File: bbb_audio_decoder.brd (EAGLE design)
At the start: 110.5 x 100 mm, 183 parts, among them IC1 OPA2134, IC2 LM317, IC3 LM337, IC4 OPA2134, IC5 OPA2134, IC6 OPA2134, P1 PLR135/T9, P9 P9, Q1 BS170, Q2 BS170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

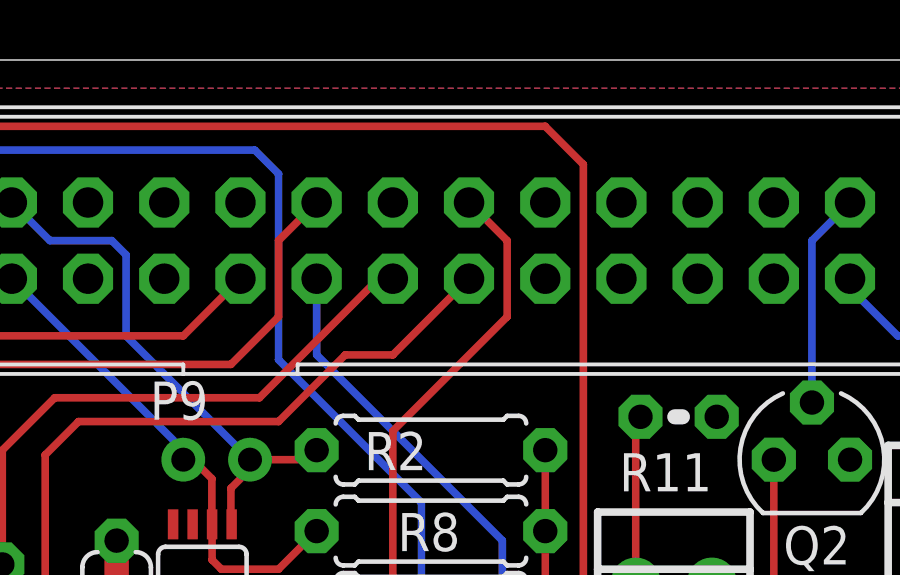
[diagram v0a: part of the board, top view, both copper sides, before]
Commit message: Fix DIR9001 DOUT wrong connection
It was wired to pin 32 in BBB P9, which is VADC. The correct pin is 30.
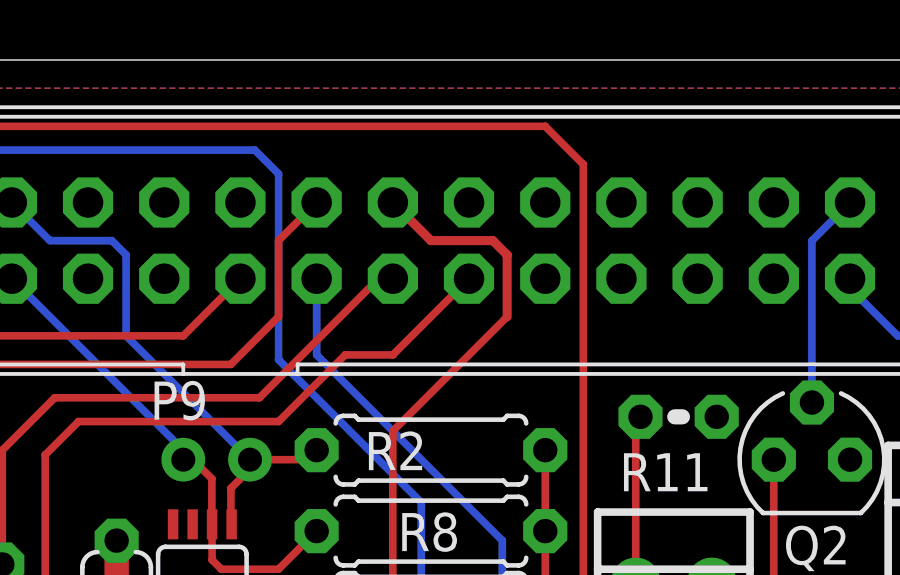
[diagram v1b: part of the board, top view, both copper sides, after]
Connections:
- net DIN: now also P9.30; no longer P9.32
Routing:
- net DIN: track 18.4 -> 20.6 mm
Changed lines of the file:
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@@
 <signal name="DIN">
 <contactref element="R32" pad="1"/>
-<contactref element="P9" pad="32"/>
-<wire x1="85.09" y1="95.25" x2="86.36" y2="93.98" width="0.254" layer="1"/>
-<wire x1="86.36" y1="93.98" x2="86.36" y2="91.44" width="0.254" layer="1"/>
+<contactref element="P9" pad="30"/>
 <wire x1="86.36" y1="91.44" x2="82.55" y2="87.63" width="0.254" layer="1"/>
 <wire x1="82.55" y1="87.63" x2="82.55" y2="81.43875" width="0.254" layer="1"/>
 <wire x1="82.55" y1="81.43875" x2="80.80375" y2="79.6925" width="0.254" layer="1"/>
+<wire x1="86.36" y1="91.44" x2="86.36" y2="93.50375" width="0.3048" layer="1"/>
+<wire x1="86.36" y1="93.50375" x2="85.88375" y2="93.98" width="0.3048" layer="1"/>
+<wire x1="85.88375" y1="93.98" x2="83.82" y2="93.98" width="0.3048" layer="1"/>
+<wire x1="83.82" y1="93.98" x2="82.55" y2="95.25" width="0.3048" layer="1"/>
 </signal>
 <signal name="N$5">

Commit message: Fixes wrong net name
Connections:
- net AHCLKX renamed FSX
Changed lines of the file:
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@@
 <wire x1="78.74" y1="93.98" x2="80.01" y2="95.25" width="0.254" layer="1"/>
 </signal>
-<signal name="AHCLKX">
+<signal name="FSX">
 <contactref element="P9" pad="29"/>
 <contactref element="R35" pad="1"/>

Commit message: Use P9 connector with wiring for slave m-clock
As described from the eaglecustom repo:

> For my purpose, I need to use an external master clock. This is input on
> ahclkr, which is pin 28. For that, the previous pin 28 function, axr2,
> has been moved to axr1, pin 41. And for that, the 'ready' LED that was
> on pin 41 has been removed.
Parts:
- removed Q1: BS170, transistor-small-signal:SOT54E
- removed R10: 120, rcl:0204V
- removed READY: 22-23-2021, con-molex:22-23-2021
- U$1: value P9 -> BEAGLEBONEP9
- renumbered P9 to U$1
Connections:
- removed net N$28: R10.1, READY.1
- removed net N$4: Q1.D, READY.2
- removed net N$93: Q1.G, U$1.41
- net DGND: no longer Q1.S
- net DOUT: now also U$1.41; no longer U$1.28
- net VDD: no longer R10.2
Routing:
- net DOUT: track 25.0 -> 40.2 mm, vias 0 -> 1
- net N$93: track 10.9 -> 0.00 mm
- net N$4: track 5.03 -> 0.00 mm
- net N$28: track 4.32 -> 0.00 mm
- net FSX: track 19.2 -> 20.7 mm
- net N$94: track 7.19 -> 8.25 mm
- net ACLKX: track 27.1 -> 27.8 mm

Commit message: Set DIR9001 SCKO to 512 * Fs
Both PSCKO pins connect to VDD. I need this to drive 8 channel TDM mode
in the mcasp in the Beagle Bone.
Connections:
- net VDD: now also U2.13, U2.14
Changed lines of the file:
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@@
 <contactref element="U$1" pad="4"/>
 <contactref element="U$1" pad="3"/>
+<contactref element="U2" pad="14"/>
+<contactref element="U2" pad="13"/>
 </signal>
 <signal name="DGND">

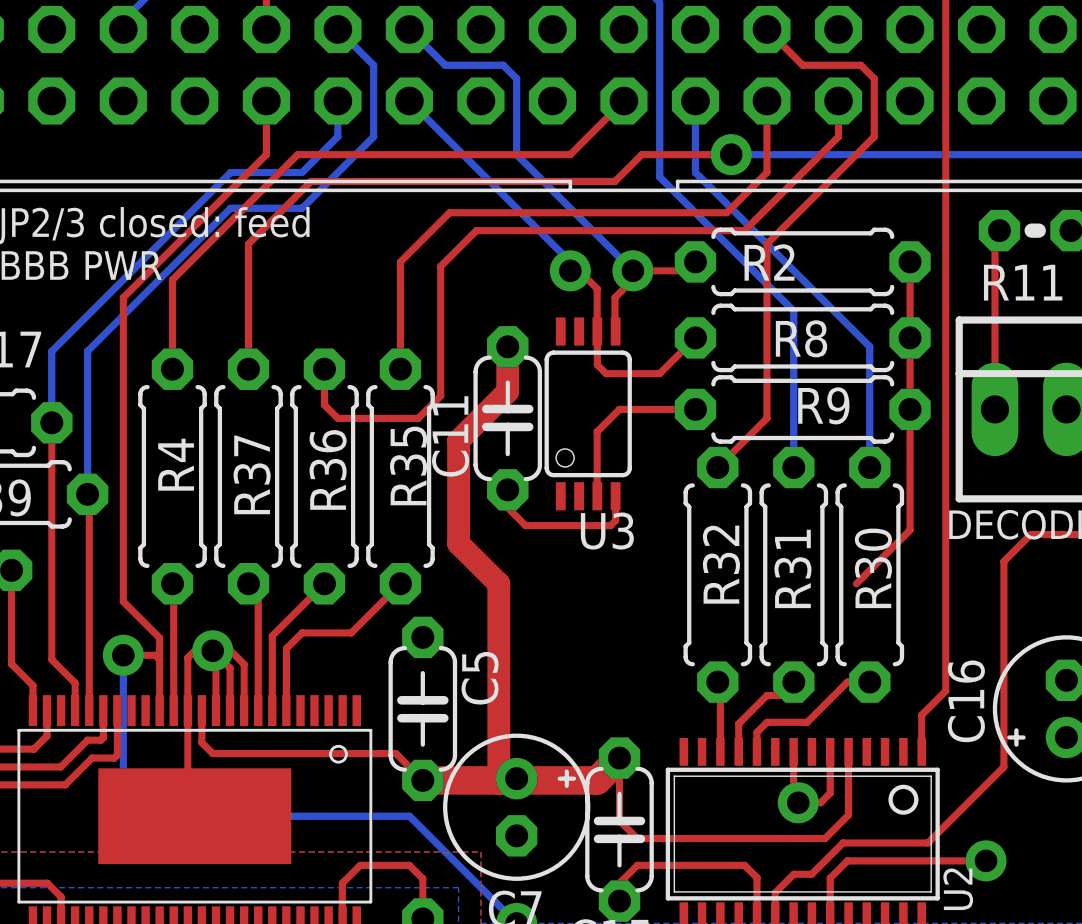
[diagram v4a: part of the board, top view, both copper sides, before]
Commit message: DIR9001 SCKO goes to input of PCM1690 and BBB
This follows commit c6b4b11003516838945a68f4a9d2063d0b8848d0; we now
actually connect the master clock.
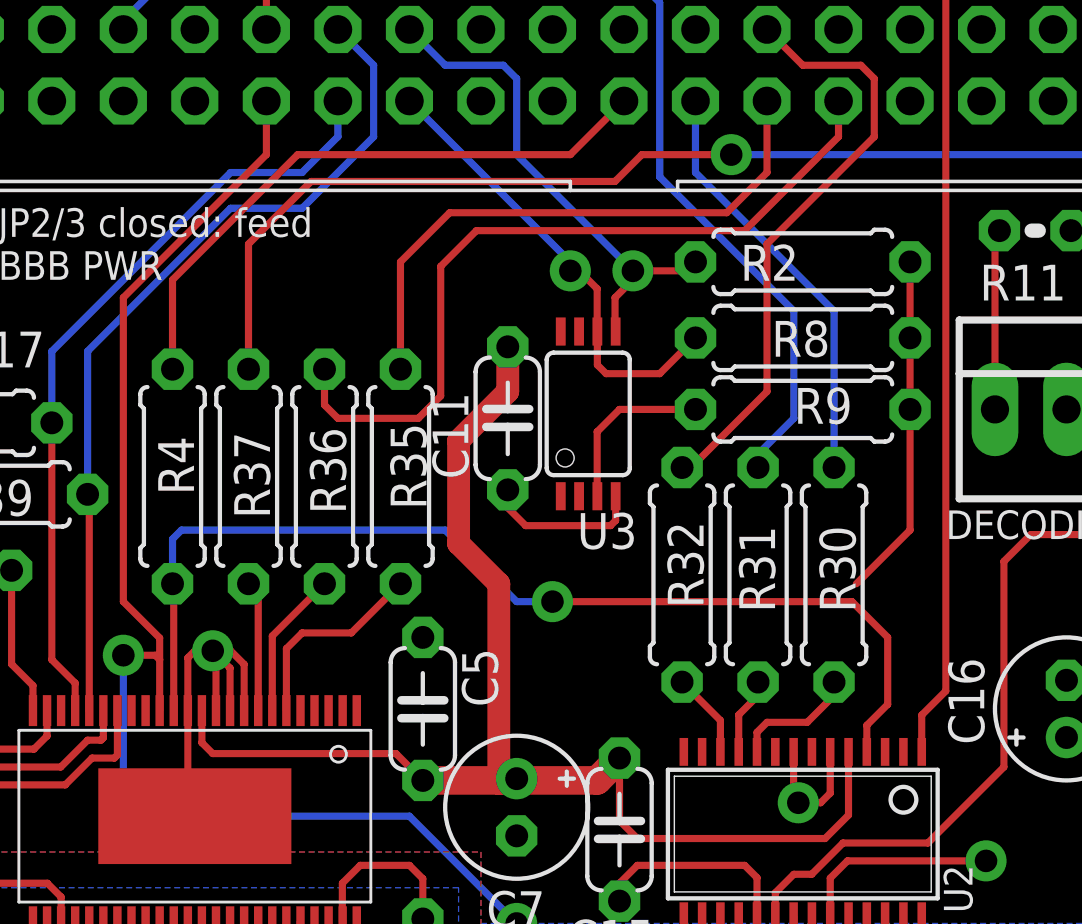
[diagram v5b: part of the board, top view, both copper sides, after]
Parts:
- moved R30 1.27 mm to (84.9, 75.9)
- moved R31 1.27 mm to (82.2, 75.9)
- moved R32 1.27 mm to (79.5, 75.9)
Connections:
- net N$5: now also U2.4
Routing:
- net N$5: track 4.52 -> 37.6 mm, vias 0 -> 1
- net N$52: track 3.57 -> 2.76 mm
- net DIN: track 20.6 -> 21.4 mm
- net ACLKR: track 38.8 -> 39.3 mm
- net N$51: track 2.52 -> 3.04 mm
- net FSR: track 15.6 -> 15.1 mm
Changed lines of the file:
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@@
 <attribute name="VALUE" x="84.455" y="60.96" size="1.27" layer="27" ratio="10" rot="R270"/>
 </element>
-<element name="R30" library="rcl" package="0207/7" value="22" x="86.20125" y="75.8825" smashed="yes" rot="R270">
-<attribute name="NAME" x="85.69325" y="77.62875" size="1.27" layer="25" ratio="10" rot="R270"/>
-<attribute name="VALUE" x="85.64245" y="78.1685" size="1.27" layer="27" ratio="10" rot="R270"/>
-</element>
-<element name="R31" library="rcl" package="0207/7" value="22" x="83.5025" y="75.8825" smashed="yes" rot="R270">
-<attribute name="NAME" x="82.83575" y="77.62875" size="1.27" layer="25" ratio="10" rot="R270"/>
-<attribute name="VALUE" x="82.9437" y="78.1685" size="1.27" layer="27" ratio="10" rot="R270"/>
-</element>
-<element name="R32" library="rcl" package="0207/7" value="22" x="80.80375" y="75.8825" smashed="yes" rot="R270">
-<attribute name="NAME" x="80.29575" y="77.7875" size="1.27" layer="25" ratio="10" rot="R270"/>
-<attribute name="VALUE" x="80.24495" y="78.1685" size="1.27" layer="27" ratio="10" rot="R270"/>
+<element name="R30" library="rcl" package="0207/7" value="22" x="84.93125" y="75.8825" smashed="yes" rot="R270">
+<attribute name="NAME" x="84.42325" y="77.62875" size="1.27" layer="25" ratio="10" rot="R270"/>
+<attribute name="VALUE" x="84.37245" y="78.1685" size="1.27" layer="27" ratio="10" rot="R270"/>
+</element>
+<element name="R31" library="rcl" package="0207/7" value="22" x="82.2325" y="75.8825" smashed="yes" rot="R270">
+<attribute name="NAME" x="81.56575" y="77.62875" size="1.27" layer="25" ratio="10" rot="R270"/>
+<attribute name="VALUE" x="81.6737" y="78.1685" size="1.27" layer="27" ratio="10" rot="R270"/>
+</element>
+<element name="R32" library="rcl" package="0207/7" value="22" x="79.53375" y="75.8825" smashed="yes" rot="R270">
+<attribute name="NAME" x="79.02575" y="77.7875" size="1.27" layer="25" ratio="10" rot="R270"/>
+<attribute name="VALUE" x="78.97495" y="78.1685" size="1.27" layer="27" ratio="10" rot="R270"/>
 </element>
 <element name="R3" library="rcl" package="0207/7" value="10k" x="51.59375" y="69.85" smashed="yes" rot="R90">
@@
 <contactref element="R32" pad="1"/>
 <wire x1="86.36" y1="91.44" x2="82.55" y2="87.63" width="0.254" layer="1"/>
-<wire x1="82.55" y1="87.63" x2="82.55" y2="81.43875" width="0.254" layer="1"/>
-<wire x1="82.55" y1="81.43875" x2="80.80375" y2="79.6925" width="0.254" layer="1"/>
+<wire x1="82.55" y1="87.63" x2="82.55" y2="82.39125" width="0.254" layer="1"/>
 <wire x1="86.36" y1="91.44" x2="86.36" y2="93.50375" width="0.254" layer="1"/>
 <wire x1="86.36" y1="93.50375" x2="85.88375" y2="93.98" width="0.254" layer="1"/>
@@
 <contactref element="U$1" pad="30"/>
 <wire x1="83.82" y1="93.98" x2="82.55" y2="95.25" width="0.254" layer="1"/>
+<wire x1="79.53375" y1="79.6925" x2="79.85125" y2="79.6925" width="0.254" layer="1"/>
+<wire x1="79.85125" y1="79.6925" x2="82.55" y2="82.39125" width="0.254" layer="1"/>
 </signal>
 <signal name="N$5">
@@
 <wire x1="61.48" y1="71.06" x2="61.48" y2="75.52125" width="0.254" layer="1"/>
 <wire x1="61.48" y1="75.52125" x2="61.43625" y2="75.565" width="0.254" layer="1"/>
+<contactref element="U2" pad="4"/>
+<wire x1="86.095" y1="69.5928" x2="86.095" y2="70.5375" width="0.254" layer="1"/>
+<wire x1="86.095" y1="70.5375" x2="86.83625" y2="71.27875" width="0.254" layer="1"/>
+<wire x1="86.83625" y1="71.27875" x2="86.83625" y2="73.66" width="0.254" layer="1"/>
+<via x="74.93" y="74.93" extent="1-16" drill="0.8" diameter="0.8128"/>
+<wire x1="74.93" y1="74.93" x2="73.66" y2="74.93" width="0.254" layer="16"/>
+<wire x1="73.66" y1="74.93" x2="71.12" y2="77.47" width="0.254" layer="16"/>
+<wire x1="71.12" y1="77.47" x2="61.75375" y2="77.47" width="0.254" layer="16"/>
+<wire x1="61.75375" y1="77.47" x2="61.43625" y2="77.1525" width="0.254" layer="16"/>
+<wire x1="61.43625" y1="77.1525" x2="61.43625" y2="75.565" width="0.254" layer="16"/>
+<wire x1="74.93" y1="74.93" x2="85.56625" y2="74.93" width="0.254" layer="1"/>
+<wire x1="85.56625" y1="74.93" x2="86.83625" y2="73.66" width="0.254" layer="1"/>
 </signal>
 <signal name="VCOM">
@@
 <contactref element="R32" pad="2"/>
 <contactref element="U2" pad="12"/>
-<wire x1="80.895" y1="69.5928" x2="80.895" y2="71.98125" width="0.254" layer="1"/>
-<wire x1="80.895" y1="71.98125" x2="80.80375" y2="72.0725" width="0.254" layer="1"/>
+<wire x1="80.895" y1="69.5928" x2="80.895" y2="70.71125" width="0.254" layer="1"/>
+<wire x1="80.895" y1="70.71125" x2="79.53375" y2="72.0725" width="0.254" layer="1"/>
 </signal>
 <signal name="N$52">
 <contactref element="R31" pad="2"/>
 <contactref element="U2" pad="11"/>
-<wire x1="81.545" y1="69.5928" x2="81.545" y2="70.59125" width="0.254" layer="1"/>
-<wire x1="81.545" y1="70.59125" x2="82.55" y2="71.59625" width="0.254" layer="1"/>
-<wire x1="82.55" y1="71.59625" x2="83.02625" y2="71.59625" width="0.254" layer="1"/>
-<wire x1="83.02625" y1="71.59625" x2="83.5025" y2="72.0725" width="0.254" layer="1"/>
+<wire x1="81.545" y1="69.5928" x2="81.545" y2="70.90875" width="0.254" layer="1"/>
+<wire x1="81.545" y1="70.90875" x2="82.2325" y2="71.59625" width="0.254" layer="1"/>
+<wire x1="82.2325" y1="71.59625" x2="82.2325" y2="72.0725" width="0.254" layer="1"/>
 </signal>
 <signal name="N$53">
@@
 <wire x1="82.55" y1="70.64375" x2="83.97875" y2="70.64375" width="0.254" layer="1"/>
 <wire x1="83.97875" y1="70.64375" x2="85.4075" y2="72.0725" width="0.254" layer="1"/>
-<wire x1="85.4075" y1="72.0725" x2="86.20125" y2="72.0725" width="0.254" layer="1"/>
+<wire x1="85.4075" y1="72.0725" x2="84.93125" y2="72.0725" width="0.254" layer="1"/>
 </signal>
 <signal name="FSR">
 <contactref element="R30" pad="1"/>
-<wire x1="86.20125" y1="79.6925" x2="86.20125" y2="83.97875" width="0.254" layer="16"/>
-<wire x1="86.20125" y1="83.97875" x2="80.01" y2="90.17" width="0.254" layer="16"/>
+<wire x1="84.93125" y1="79.6925" x2="84.93125" y2="85.24875" width="0.254" layer="16"/>
+<wire x1="84.93125" y1="85.24875" x2="80.01" y2="90.17" width="0.254" layer="16"/>
 <contactref element="U$1" pad="27"/>
 <wire x1="80.01" y1="90.17" x2="80.01" y2="92.71" width="0.254" layer="16"/>
@@
 <wire x1="78.74" y1="96.2025" x2="78.74" y2="90.01125" width="0.254" layer="16"/>
 <wire x1="78.74" y1="90.01125" x2="83.5025" y2="85.24875" width="0.254" layer="16"/>
-<wire x1="83.5025" y1="85.24875" x2="83.5025" y2="79.6925" width="0.254" layer="16"/>
+<wire x1="83.5025" y1="85.24875" x2="83.5025" y2="81.43875" width="0.254" layer="16"/>
+<wire x1="83.5025" y1="81.43875" x2="82.2325" y2="80.16875" width="0.254" layer="16"/>
+<wire x1="82.2325" y1="80.16875" x2="82.2325" y2="79.6925" width="0.254" layer="16"/>
 <wire x1="59.69" y1="95.5675" x2="61.11875" y2="96.99625" width="0.254" layer="16"/>
 <wire x1="61.11875" y1="96.99625" x2="77.94625" y2="96.99625" width="0.254" layer="16"/>
